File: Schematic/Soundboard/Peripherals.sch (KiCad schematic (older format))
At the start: 19 parts, among them J8 Micro_SD_Card, SW2 SW_Push, SW3 SW_Push, SW4 SW_Push, SW5 SW_Push, U10 W25Q128JVS, U11 BMI160

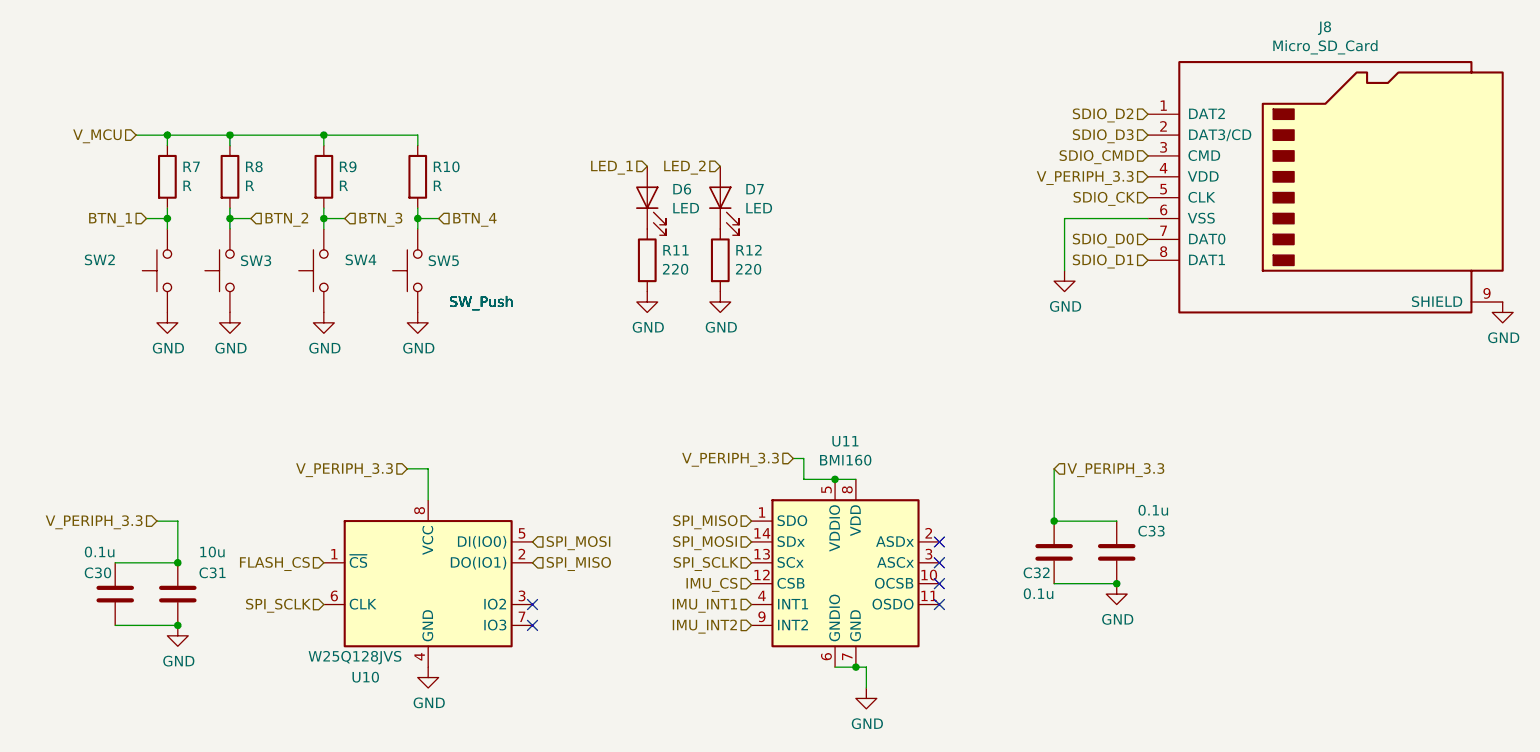
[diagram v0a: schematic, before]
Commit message: Complete connections except for display to be chosen
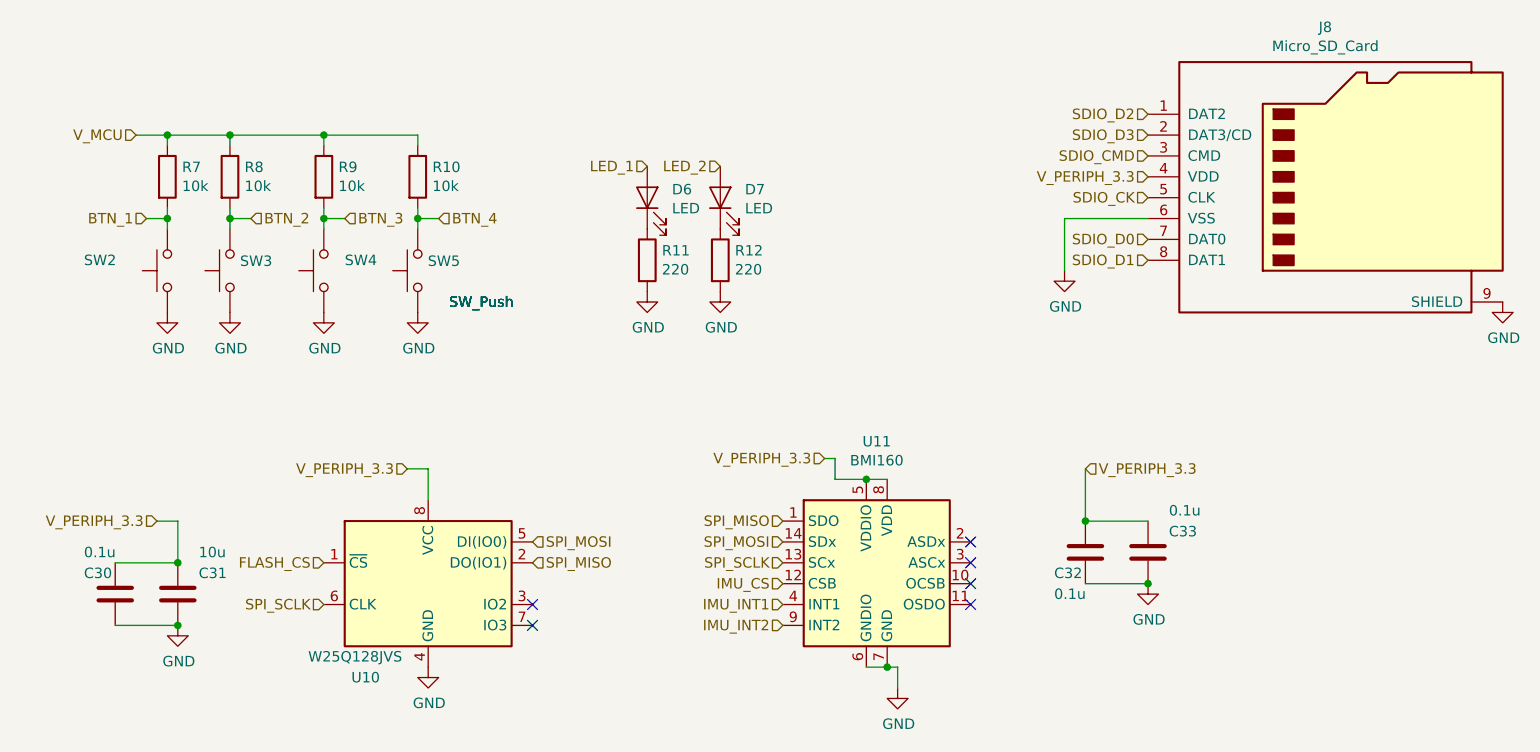
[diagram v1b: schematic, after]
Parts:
- R10, R7, R8, R9: value R -> 10k
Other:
- moved on the sheet: C32, C33, U11
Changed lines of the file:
@@
 L Soundboard-rescue:BMI160-Sensor_Motion U?
 U 1 1 5F4F02AE
-P 6450 4150
+P 6600 4150
 AR Path="/5F0E03BF/5F4F02AE" Ref="U?"  Part="1"
 AR Path="/5F4E88D1/5F4F02AE" Ref="U11"  Part="1"
-F 0 "U11" H 6400 4731 50  0000 C CNN
-F 1 "BMI160" H 6400 4640 50  0000 C CNN
-F 2 "Package_LGA:Bosch_LGA-14_3x2.5mm_P0.5mm" H 6450 4150 50  0001 C CNN
-F 3 "https://ae-bst.resource.bosch.com/media/_tech/media/datasheets/BST-BMI160-DS000.pdf" H 5750 5000 50  0001 C CNN
-	1    6450 4150
-	1    0    0    -1
-$EndComp
-Wire Wire Line
-	6350 4650 6450 4650
-Wire Wire Line
-	6500 4650 6500 4750
-Connection ~ 6450 4650
-Wire Wire Line
-	6450 4650 6500 4650
+F 0 "U11" H 6550 4731 50  0000 C CNN
+F 1 "BMI160" H 6550 4640 50  0000 C CNN
+F 2 "Package_LGA:Bosch_LGA-14_3x2.5mm_P0.5mm" H 6600 4150 50  0001 C CNN
+F 3 "https://ae-bst.resource.bosch.com/media/_tech/media/datasheets/BST-BMI160-DS000.pdf" H 5900 5000 50  0001 C CNN
+	1    6600 4150
+	1    0    0    -1
+$EndComp
+Wire Wire Line
+	6500 4650 6600 4650
+Wire Wire Line
+	6650 4650 6650 4750
+Connection ~ 6600 4650
+Wire Wire Line
+	6600 4650 6650 4650
 $Comp
 L power:GND #PWR?
 U 1 1 5F4F02BC
-P 6500 4750
+P 6650 4750
 AR Path="/5F0E03BF/5F4F02BC" Ref="#PWR?"  Part="1"
 AR Path="/5F4E88D1/5F4F02BC" Ref="#PWR035"  Part="1"
-F 0 "#PWR035" H 6500 4500 50  0001 C CNN
-F 1 "GND" H 6505 4577 50  0000 C CNN
-F 2 "" H 6500 4750 50  0001 C CNN
-F 3 "" H 6500 4750 50  0001 C CNN
-	1    6500 4750
-	1    0    0    -1
-$EndComp
-NoConn ~ 6850 4050
-NoConn ~ 6850 4150
-NoConn ~ 6850 4250
-NoConn ~ 6850 4350
-Wire Wire Line
-	6350 3750 6450 3750
+F 0 "#PWR035" H 6650 4500 50  0001 C CNN
+F 1 "GND" H 6655 4577 50  0000 C CNN
+F 2 "" H 6650 4750 50  0001 C CNN
+F 3 "" H 6650 4750 50  0001 C CNN
+	1    6650 4750
+	1    0    0    -1
+$EndComp
+NoConn ~ 7000 4050
+NoConn ~ 7000 4150
+NoConn ~ 7000 4250
+NoConn ~ 7000 4350
+Wire Wire Line
+	6500 3750 6600 3750
 $Comp
 L Soundboard-rescue:W25Q128JVS-Memory_Flash U?
@@
 L Device:C C?
 U 1 1 5F4F02CF
-P 7400 4100
+P 7550 4100
 AR Path="/5F0E03BF/5F4F02CF" Ref="C?"  Part="1"
 AR Path="/5F4E88D1/5F4F02CF" Ref="C32"  Part="1"
-F 0 "C32" H 7250 4000 50  0000 L CNN
-F 1 "0.1u" H 7250 3900 50  0000 L CNN
-F 2 "Capacitor_SMD:C_0603_1608Metric_Pad1.05x0.95mm_HandSolder" H 7438 3950 50  0001 C CNN
-F 3 "~" H 7400 4100 50  0001 C CNN
-	1    7400 4100
+F 0 "C32" H 7400 4000 50  0000 L CNN
+F 1 "0.1u" H 7400 3900 50  0000 L CNN
+F 2 "Capacitor_SMD:C_0603_1608Metric_Pad1.05x0.95mm_HandSolder" H 7588 3950 50  0001 C CNN
+F 3 "~" H 7550 4100 50  0001 C CNN
+	1    7550 4100
 	1    0    0    -1
 $EndComp
@@
 L Device:C C?
 U 1 1 5F4F02D6
-P 7700 4100
+P 7850 4100
 AR Path="/5F0E03BF/5F4F02D6" Ref="C?"  Part="1"
 AR Path="/5F4E88D1/5F4F02D6" Ref="C33"  Part="1"
-F 0 "C33" H 7800 4200 50  0000 L CNN
-F 1 "0.1u" H 7800 4300 50  0000 L CNN
-F 2 "Capacitor_SMD:C_0603_1608Metric_Pad1.05x0.95mm_HandSolder" H 7738 3950 50  0001 C CNN
-F 3 "~" H 7700 4100 50  0001 C CNN
-	1    7700 4100
-	1    0    0    -1
-$EndComp
-Wire Wire Line
-	7400 3950 7700 3950
-Wire Wire Line
-	7700 4250 7400 4250
+F 0 "C33" H 7950 4200 50  0000 L CNN
+F 1 "0.1u" H 7950 4300 50  0000 L CNN
+F 2 "Capacitor_SMD:C_0603_1608Metric_Pad1.05x0.95mm_HandSolder" H 7888 3950 50  0001 C CNN
+F 3 "~" H 7850 4100 50  0001 C CNN
+	1    7850 4100
+	1    0    0    -1
+$EndComp
+Wire Wire Line
+	7550 3950 7850 3950
+Wire Wire Line
+	7850 4250 7550 4250
 $Comp
 L power:GND #PWR?
 U 1 1 5F4F02DF
-P 7700 4250
+P 7850 4250
 AR Path="/5F0E03BF/5F4F02DF" Ref="#PWR?"  Part="1"
 AR Path="/5F4E88D1/5F4F02DF" Ref="#PWR037"  Part="1"
-F 0 "#PWR037" H 7700 4000 50  0001 C CNN
-F 1 "GND" H 7705 4077 50  0000 C CNN
-F 2 "" H 7700 4250 50  0001 C CNN
-F 3 "" H 7700 4250 50  0001 C CNN
-	1    7700 4250
-	1    0    0    -1
-$EndComp
-Connection ~ 7700 4250
+F 0 "#PWR037" H 7850 4000 50  0001 C CNN
+F 1 "GND" H 7855 4077 50  0000 C CNN
+F 2 "" H 7850 4250 50  0001 C CNN
+F 3 "" H 7850 4250 50  0001 C CNN
+	1    7850 4250
+	1    0    0    -1
+$EndComp
+Connection ~ 7850 4250
 $Comp
 L power:GND #PWR?
@@
 	3200 3950 3200 4150
 Connection ~ 3200 4150
-Text HLabel 6150 3650 0    50   Input ~ 0
+Text HLabel 6300 3650 0    50   Input ~ 0
 V_PERIPH_3.3
 Wire Wire Line
-	6150 3650 6200 3650
-Wire Wire Line
-	6200 3650 6200 3750
-Wire Wire Line
-	6200 3750 6350 3750
-Connection ~ 6350 3750
-Text HLabel 7400 3700 2    50   Input ~ 0
+	6300 3650 6350 3650
+Wire Wire Line
+	6350 3650 6350 3750
+Wire Wire Line
+	6350 3750 6500 3750
+Connection ~ 6500 3750
+Text HLabel 7550 3700 2    50   Input ~ 0
 V_PERIPH_3.3
-Connection ~ 7400 3950
-Wire Wire Line
-	7400 3700 7400 3950
+Connection ~ 7550 3950
+Wire Wire Line
+	7550 3700 7550 3950
 Connection ~ 3200 4450
 $Comp
@@
 AR Path="/5F4E88D1/5F4F2E71" Ref="R7"  Part="1"
 F 0 "R7" H 3220 2346 50  0000 L CNN
-F 1 "R" H 3220 2255 50  0000 L CNN
+F 1 "10k" H 3220 2255 50  0000 L CNN
 F 2 "" V 3080 2300 50  0001 C CNN
 F 3 "~" H 3150 2300 50  0001 C CNN
@@
 AR Path="/5F4E88D1/5F4F2E78" Ref="R8"  Part="1"
 F 0 "R8" H 3520 2346 50  0000 L CNN
-F 1 "R" H 3520 2255 50  0000 L CNN
+F 1 "10k" H 3520 2255 50  0000 L CNN
 F 2 "" V 3380 2300 50  0001 C CNN
 F 3 "~" H 3450 2300 50  0001 C CNN
@@
 AR Path="/5F4E88D1/5F4F2EA4" Ref="R9"  Part="1"
 F 0 "R9" H 3970 2346 50  0000 L CNN
-F 1 "R" H 3970 2255 50  0000 L CNN
+F 1 "10k" H 3970 2255 50  0000 L CNN
 F 2 "" V 3830 2300 50  0001 C CNN
 F 3 "~" H 3900 2300 50  0001 C CNN
@@
 AR Path="/5F4E88D1/5F4F2EAB" Ref="R10"  Part="1"
 F 0 "R10" H 4420 2346 50  0000 L CNN
-F 1 "R" H 4420 2255 50  0000 L CNN
+F 1 "10k" H 4420 2255 50  0000 L CNN
 F 2 "" V 4280 2300 50  0001 C CNN
 F 3 "~" H 4350 2300 50  0001 C CNN
@@
 	4350 2100 4350 2150
 Connection ~ 3900 2100
-Text HLabel 5950 4350 0    50   Input ~ 0
+Text HLabel 6100 4350 0    50   Input ~ 0
 IMU_INT1
-Text HLabel 5950 4450 0    50   Input ~ 0
+Text HLabel 6100 4450 0    50   Input ~ 0
 IMU_INT2
-Text HLabel 5950 4250 0    50   Input ~ 0
+Text HLabel 6100 4250 0    50   Input ~ 0
 IMU_CS
-Text HLabel 5950 3950 0    50   Input ~ 0
+Text HLabel 6100 3950 0    50   Input ~ 0
 SPI_MISO
-Text HLabel 5950 4050 0    50   Input ~ 0
+Text HLabel 6100 4050 0    50   Input ~ 0
 SPI_MOSI
-Text HLabel 5950 4150 0    50   Input ~ 0
+Text HLabel 6100 4150 0    50   Input ~ 0
 SPI_SCLK
 Text HLabel 4900 4150 2    50   Input ~ 0

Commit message: Choose display. Complete schematic
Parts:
- R10, R7, R8, R9: footprint (none) -> Resistor_SMD:R_0603_1608Metric_Pad1.05x0.95mm_HandSolder
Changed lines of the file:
@@
 $Descr A4 11693 8268
 encoding utf-8
-Sheet 7 7
+Sheet 6 7
 Title ""
 Date ""
@@
 F 0 "R7" H 3220 2346 50  0000 L CNN
 F 1 "10k" H 3220 2255 50  0000 L CNN
-F 2 "" V 3080 2300 50  0001 C CNN
+F 2 "Resistor_SMD:R_0603_1608Metric_Pad1.05x0.95mm_HandSolder" V 3080 2300 50  0001 C CNN
 F 3 "~" H 3150 2300 50  0001 C CNN
 	1    3150 2300
@@
 F 0 "R8" H 3520 2346 50  0000 L CNN
 F 1 "10k" H 3520 2255 50  0000 L CNN
-F 2 "" V 3380 2300 50  0001 C CNN
+F 2 "Resistor_SMD:R_0603_1608Metric_Pad1.05x0.95mm_HandSolder" V 3380 2300 50  0001 C CNN
 F 3 "~" H 3450 2300 50  0001 C CNN
 	1    3450 2300
@@
 F 0 "R9" H 3970 2346 50  0000 L CNN
 F 1 "10k" H 3970 2255 50  0000 L CNN
-F 2 "" V 3830 2300 50  0001 C CNN
+F 2 "Resistor_SMD:R_0603_1608Metric_Pad1.05x0.95mm_HandSolder" V 3830 2300 50  0001 C CNN
 F 3 "~" H 3900 2300 50  0001 C CNN
 	1    3900 2300
@@
 F 0 "R10" H 4420 2346 50  0000 L CNN
 F 1 "10k" H 4420 2255 50  0000 L CNN
-F 2 "" V 4280 2300 50  0001 C CNN
+F 2 "Resistor_SMD:R_0603_1608Metric_Pad1.05x0.95mm_HandSolder" V 4280 2300 50  0001 C CNN
 F 3 "~" H 4350 2300 50  0001 C CNN
 	1    4350 2300
